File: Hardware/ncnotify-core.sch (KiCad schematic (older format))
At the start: 43 parts, among them J1 5-1634503-1, J2 TC2030-CTX, J3 USB4110-GF-A, Q1 NX3008NBKS, SW1 SW_Push, SW2 SW_Push, U1 STM32L422CBT6, U2 TLV71333PDBV, U3 USBLC6-2SC6, X1 SMTU1632-LF, Y1 Q13FC1350000400

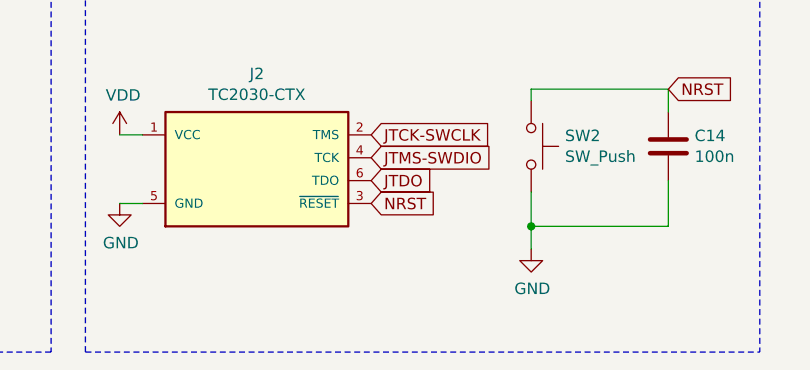
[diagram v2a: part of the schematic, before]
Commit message: Routing and replaced USB ESD chip
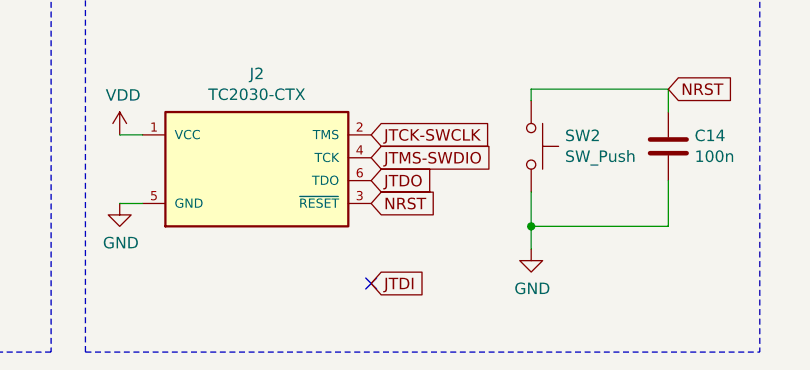
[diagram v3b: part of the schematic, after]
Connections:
- no-connect marks 28 -> 29
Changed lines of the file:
@@
 Text GLabel 5050 3250 0    50   Input ~ 0
 CONN_D-
+Text GLabel 5100 7450 2    50   Input ~ 0
+JTDI
+NoConn ~ 5100 7450
 $EndSCHEMATC

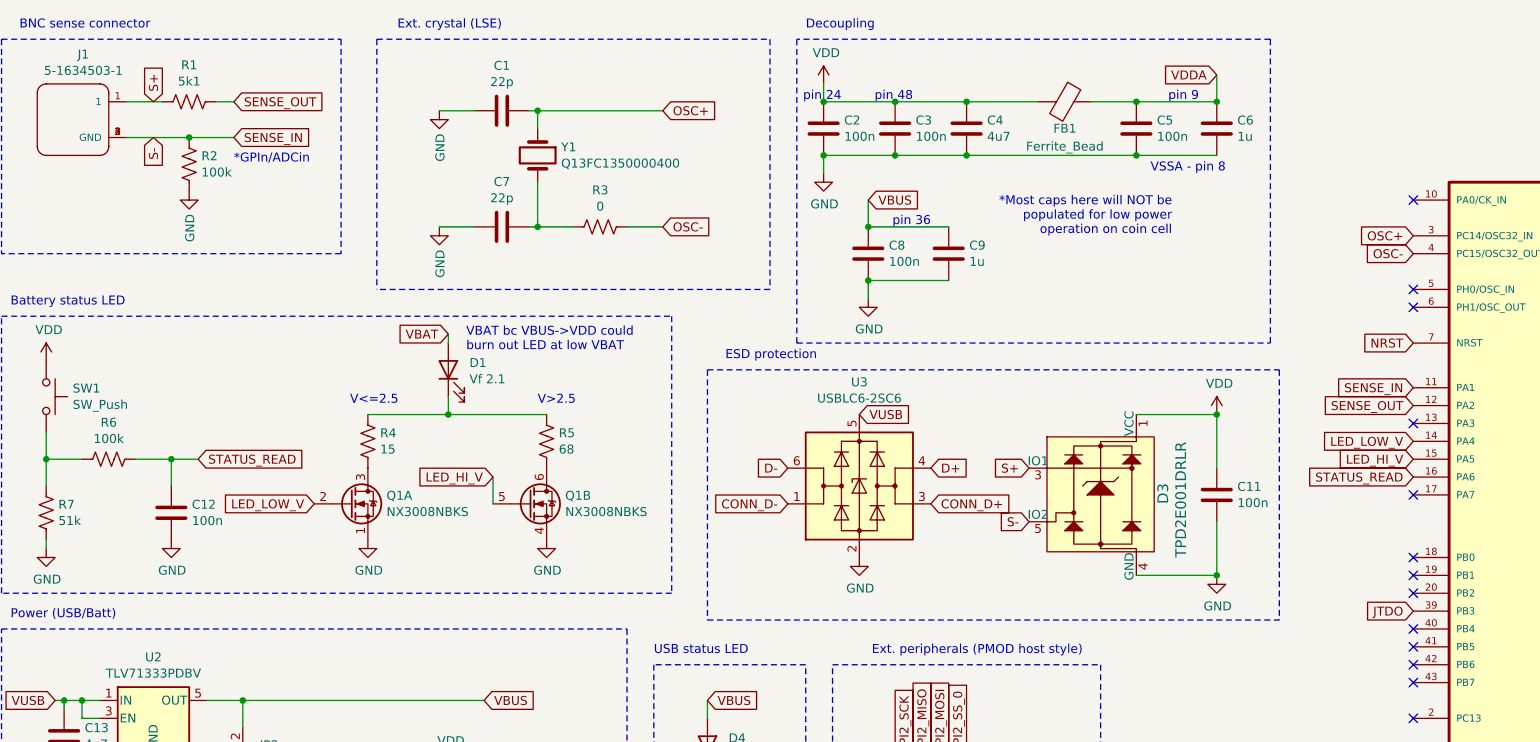
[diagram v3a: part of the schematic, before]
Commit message: lcsc part numbers for bom, cleanup before trying gerbers
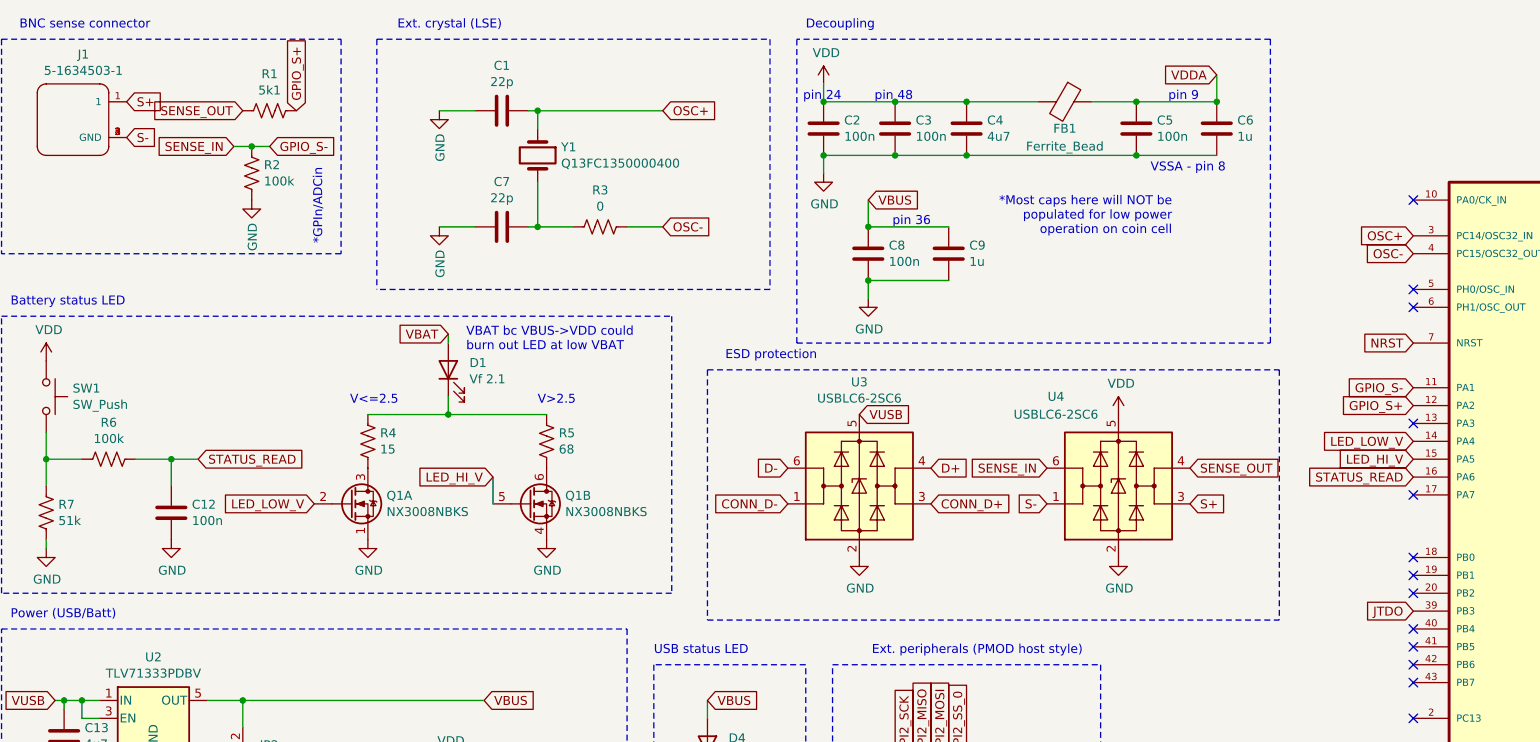
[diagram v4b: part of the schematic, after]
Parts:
- removed C11: 100n, Capacitor_SMD:C_0402_1005Metric, symbol Device:C
- removed D3: TPD2E001DRLR, digikey-footprints:SOT-553, symbol dk_TVS-Diodes:TPD2E001DRLR
- added U4: USBLC6-2SC6, Package_TO_SOT_SMD:SOT-23-6, symbol Power_Protection:USBLC6-2SC6
- C1, C7: LCSC Part # (none) -> C1555
- C12, C14, C2, C3, C5, C8: LCSC Part # (none) -> C1525
- C13, C4: LCSC Part # (none) -> C19666
- C6, C9: LCSC Part # (none) -> C52923
- D1, D4: LCSC Part # (none) -> C72038
- FB1: LCSC Part # (none) -> C1015
- J1, J2, J3, JP1, JP2, JP3, X1: LCSC Part # (none) -> DNF
- Q1: LCSC Part # (none) -> C396098
- R1, R13, R14: LCSC Part # (none) -> C25905
- R10, R7, R9: LCSC Part # (none) -> C25794
- R2, R6: LCSC Part # (none) -> C25741
- R3: LCSC Part # (none) -> C17168
- R4: LCSC Part # (none) -> C22810
- R5, R8: LCSC Part # (none) -> C27592
- SW1, SW2: LCSC Part # (none) -> C318884
- U1: LCSC Part # (none) -> C94785
- U2: LCSC Part # (none) -> C90840
- U3: LCSC Part # (none) -> C7519
- Y1: LCSC Part # (none) -> C32346
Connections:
- net GND: now also U4.2 (GND)
- net S+: now also U4.3 (I/O2); no longer R1.2
- net S-: now also U4.1 (I/O1); no longer R2.2, U1.11 (PA1)
- net SENSE_OUT: now also R1.2, U4.4 (I/O2); no longer R1.1, U1.12 (PA2)
- net VDD: now also U4.5 (VBUS)
- new net GPIO_S+: R1.1, U1.12 (PA2)
- new net GPIO_S-: R2.2, U1.11 (PA1), U4.6 (I/O1)
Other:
- moved on the sheet: R1, R2

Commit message: Cleanup silkscreen, add part numbers to sch bom
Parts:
- J1, J2, J3, JP1, JP2, JP3, X1: LCSC Part # DNF -> (none)
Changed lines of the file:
@@
 F 8 "RENATA" H 2500 4900 50  0001 L CNN "Manufacturer_Name"
 F 9 "SMTU1632-LF" H 2500 4800 50  0001 L CNN "Manufacturer_Part_Number"
-F 10 "DNF" H 1850 5400 50  0001 C CNN "LCSC Part #"
+F 10 "" H 1850 5400 50  0001 C CNN "LCSC Part #"
 	1    1850 5400
 	-1   0    0    -1
@@
 F 5 "1" H 1050 1100 50  0001 L BNN "Number_of_Positions"
 F 6 "5-1634503-1" H 1050 1100 50  0001 L BNN "Comment"
-F 7 "DNF" H 1050 1100 50  0001 C CNN "LCSC Part #"
+F 7 "" H 1050 1100 50  0001 C CNN "LCSC Part #"
 	1    1050 1100
 	1    0    0    -1
@@
 F 6 "GCT" H 2050 6700 50  0001 L BNN "MANUFACTURER"
 F 7 "Manufacturer Recommendations" H 2050 6700 50  0001 L BNN "STANDARD"
-F 8 "DNF" H 2050 6700 50  0001 C CNN "LCSC Part #"
+F 8 "" H 2050 6700 50  0001 C CNN "LCSC Part #"
 	1    2050 6700
 	1    0    0    -1
@@
 F 2 "Jumper:SolderJumper-2_P1.3mm_Open_TrianglePad1.0x1.5mm" H 2000 4650 50  0001 C CNN
 F 3 "~" H 2000 4650 50  0001 C CNN
-F 4 "DNF" H 2000 4650 50  0001 C CNN "LCSC Part #"
+F 4 "" H 2000 4650 50  0001 C CNN "LCSC Part #"
 	1    2000 4650
 	0    -1   -1   0
@@
 F 2 "Jumper:SolderJumper-2_P1.3mm_Open_TrianglePad1.0x1.5mm" H 2000 5100 50  0001 C CNN
 F 3 "~" H 2000 5100 50  0001 C CNN
-F 4 "DNF" H 2000 5100 50  0001 C CNN "LCSC Part #"
+F 4 "" H 2000 5100 50  0001 C CNN "LCSC Part #"
 	1    2000 5100
 	0    1    1    0
@@
 F 2 "libs:TC2030-IDC-NL" H 4600 6900 50  0001 C CNN
 F 3 "" H 4600 6900 50  0001 L BNN
-F 4 "DNF" H 4600 6900 50  0001 C CNN "LCSC Part #"
+F 4 "" H 4600 6900 50  0001 C CNN "LCSC Part #"
 	1    4600 6900
 	1    0    0    -1
@@
 F 2 "Connector_PinHeader_1.27mm:PinHeader_1x02_P1.27mm_Vertical" H 8100 5300 50  0001 C CNN
 F 3 "~" H 8100 5300 50  0001 C CNN
-F 4 "DNF" H 8100 5300 50  0001 C CNN "LCSC Part #"
+F 4 "" H 8100 5300 50  0001 C CNN "LCSC Part #"
 	1    8100 5300
 	0    -1   -1   0

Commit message: bump to developing version v1.1
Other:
- note added: "v1.1"
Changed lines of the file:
@@
 	2150 1250 2050 1250
 Connection ~ 2050 1250
+Text Notes 10700 7650 0    50   ~ 0
+v1.1
 $EndSCHEMATC

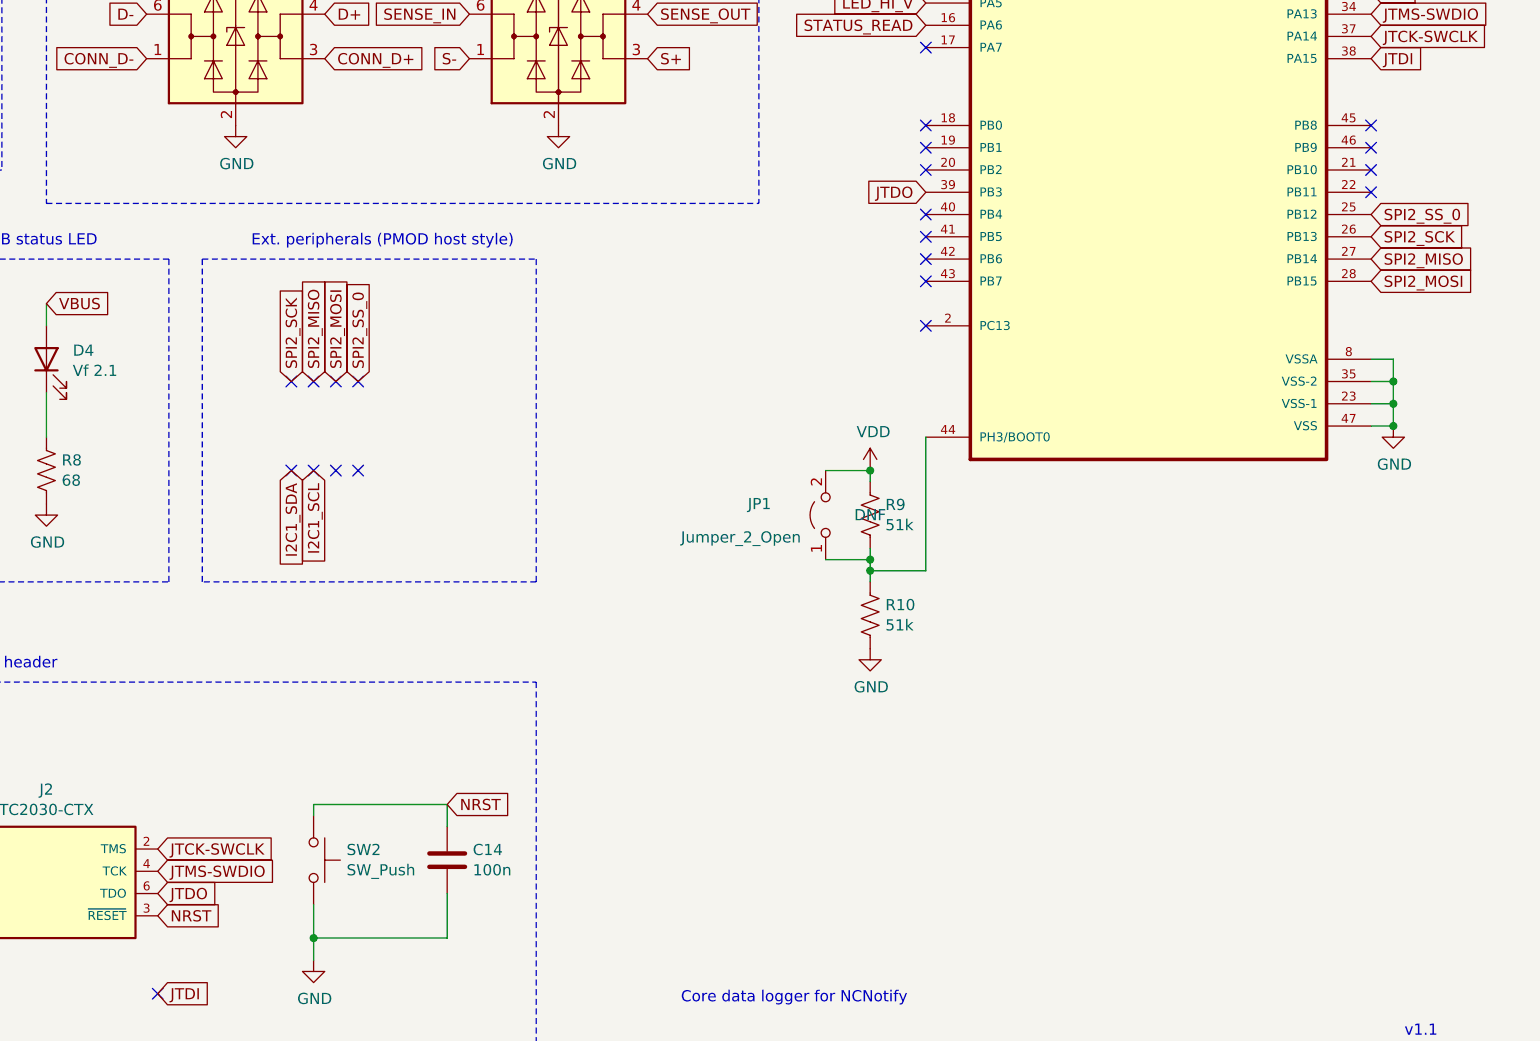
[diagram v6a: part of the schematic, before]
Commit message: Fix SWD CLK/DIO pin swap, add UART test points
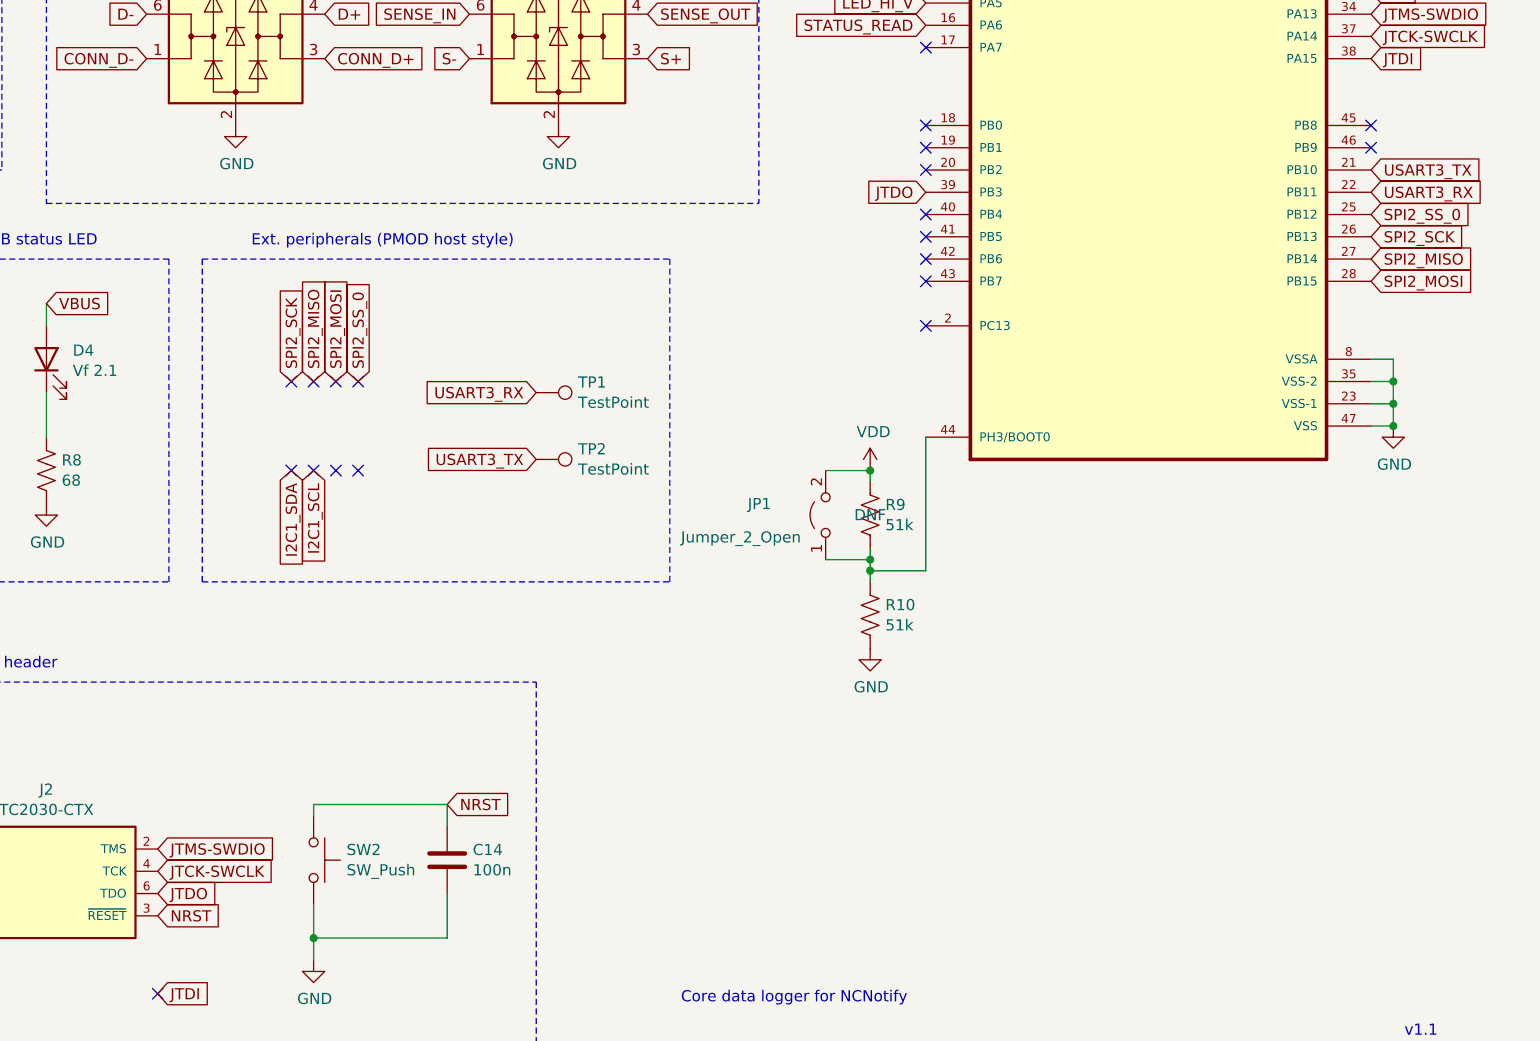
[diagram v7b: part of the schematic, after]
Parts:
- added TP1, TP2: TestPoint, TestPoint:TestPoint_Pad_D1.5mm, symbol Connector:TestPoint
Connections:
- net JTCK-SWCLK: now also J2.4 (TCK); no longer J2.2 (TMS)
- net JTMS-SWDIO: now also J2.2 (TMS); no longer J2.4 (TCK)
- net USART3_TX: now reaches U1.21 (PB10)
- net USART3_TX: now also TP2.1
- net USART3_RX: now reaches U1.22 (PB11)
- net USART3_RX: now also TP1.1
- no-connect marks 29 -> 27
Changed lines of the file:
@@
 Wire Notes Line
 	650  650  2550 650
-Text GLabel 5100 6900 2    50   Input ~ 0
+Text GLabel 5100 6800 2    50   Input ~ 0
 JTMS-SWDIO
 Text GLabel 10550 3050 2    50   Input ~ 0
@@
 Text GLabel 10550 3150 2    50   Input ~ 0
 JTCK-SWCLK
-Text GLabel 5100 6800 2    50   Input ~ 0
+Text GLabel 5100 6900 2    50   Input ~ 0
 JTCK-SWCLK
 Text GLabel 10550 3250 2    50   Input ~ 0
@@
 Ext. peripherals (PMOD host style)
 Wire Notes Line
-	5300 4150 6800 4150
-Wire Notes Line
-	6800 4150 6800 5600
-Wire Notes Line
-	6800 5600 5300 5600
+	7400 4150 7400 5600
 Wire Notes Line
 	5300 5600 5300 4150
@@
 NoConn ~ 10550 3550
 NoConn ~ 10550 3650
-NoConn ~ 10550 3750
-NoConn ~ 10550 3850
 NoConn ~ 8550 4450
 NoConn ~ 8550 4250
@@
 Text Notes 10700 7650 0    50   ~ 0
 v1.1
+Text GLabel 10550 3750 2    50   Input ~ 0
+USART3_TX
+Text GLabel 10550 3850 2    50   Input ~ 0
+USART3_RX
+$Comp
+L Connector:TestPoint TP2
+U 1 1 5FC86710
+P 6800 5050
+F 0 "TP2" V 6754 5238 50  0000 L CNN
+F 1 "TestPoint" V 6845 5238 50  0000 L CNN
+F 2 "TestPoint:TestPoint_Pad_D1.5mm" H 7000 5050 50  0001 C CNN
+F 3 "~" H 7000 5050 50  0001 C CNN
+	1    6800 5050
+	0    1    1    0
+$EndComp
+Wire Notes Line
+	5300 4150 7400 4150
+Wire Notes Line
+	5300 5600 7400 5600
+Text GLabel 6800 5050 0    50   Input ~ 0
+USART3_TX
+Text GLabel 6800 4750 0    50   Input ~ 0
+USART3_RX
+$Comp
+L Connector:TestPoint TP1
+U 1 1 5FC90D8F
+P 6800 4750
+F 0 "TP1" V 6754 4938 50  0000 L CNN
+F 1 "TestPoint" V 6845 4938 50  0000 L CNN
+F 2 "TestPoint:TestPoint_Pad_D1.5mm" H 7000 4750 50  0001 C CNN
+F 3 "~" H 7000 4750 50  0001 C CNN
+	1    6800 4750
+	0    1    1    0
+$EndComp
 $EndSCHEMATC
